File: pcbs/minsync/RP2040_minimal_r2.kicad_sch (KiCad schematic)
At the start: 43 parts, among them J1 SWD_JST, J5 SWD_HEADERS, J6 Conn_01x01_Pin, J7 SSD1306, SW1 SW_Push, U1 NCP1117-3.3_SOT223, U2 W25Q128JVS, U3 RP2040, U4 Si5351A-B-GT, Y2 Crystal_GND24

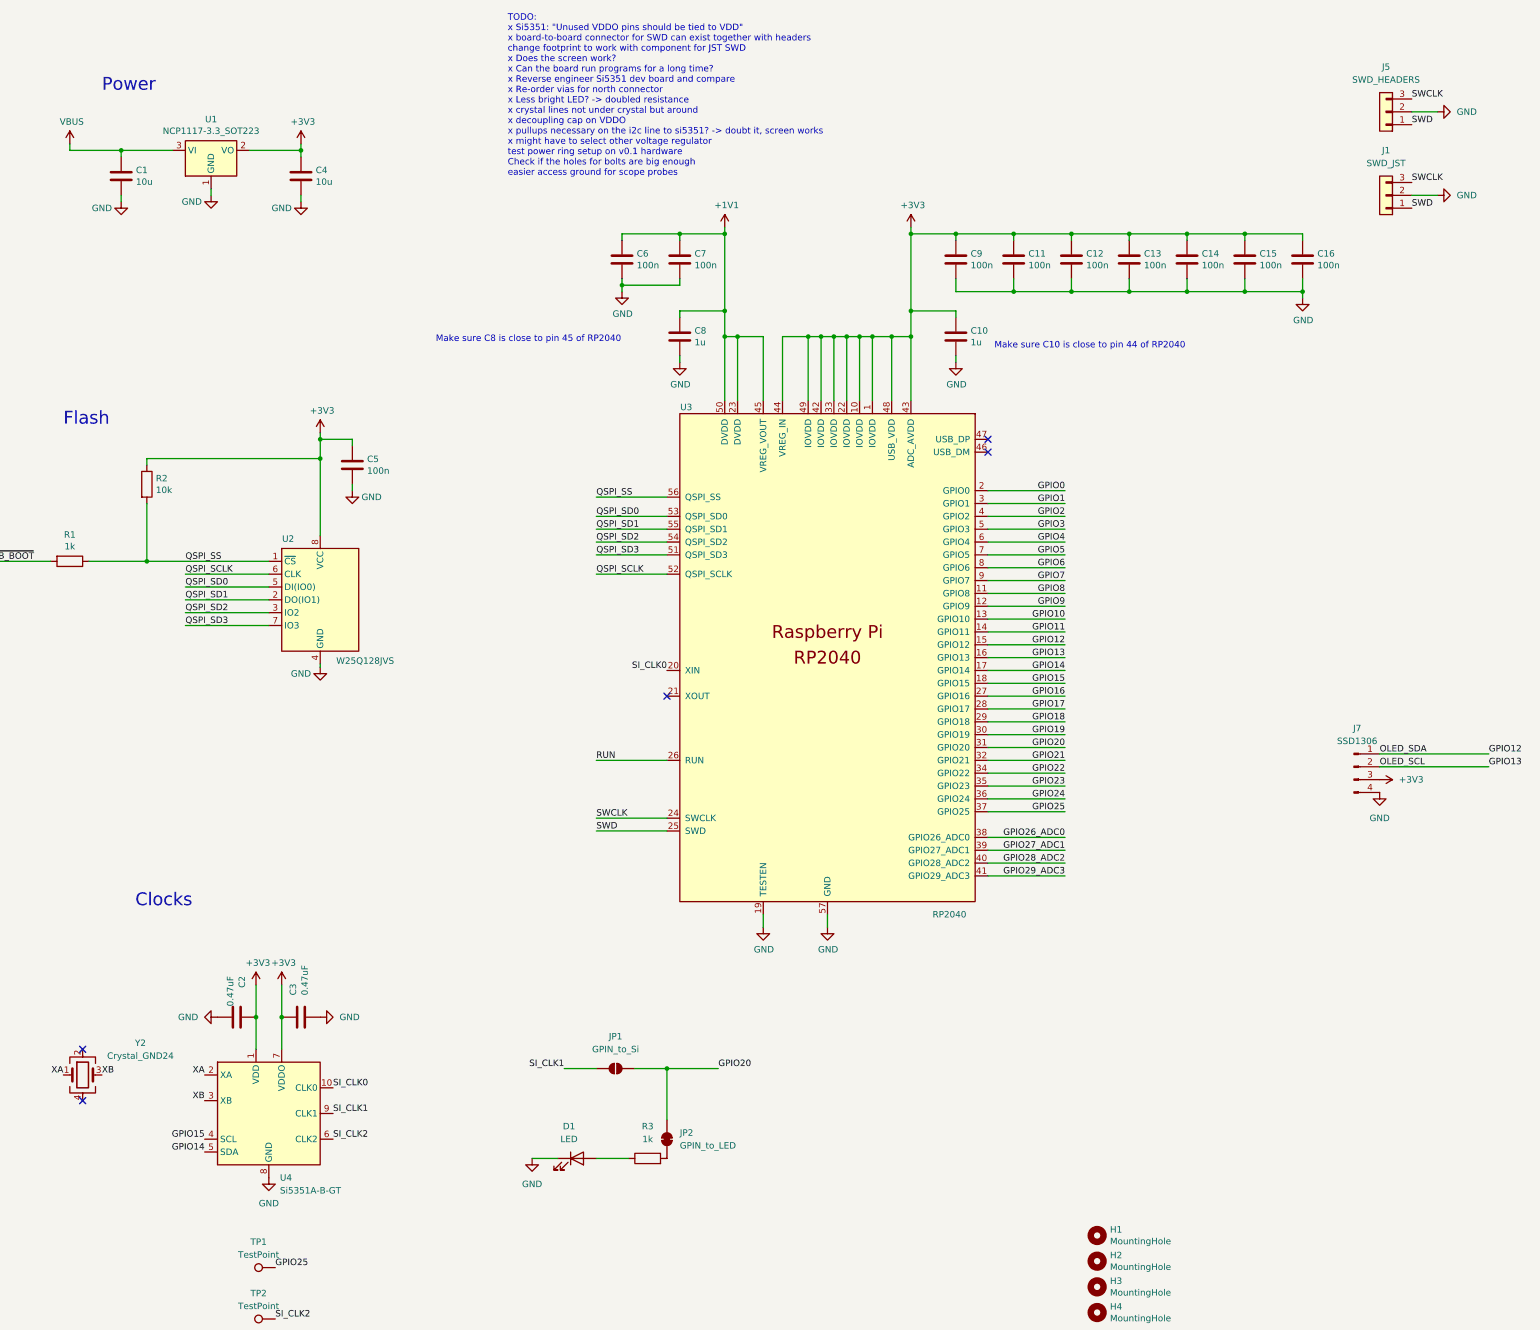
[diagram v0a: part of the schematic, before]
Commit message: Add pullups for si5351, change SWD plug footprint
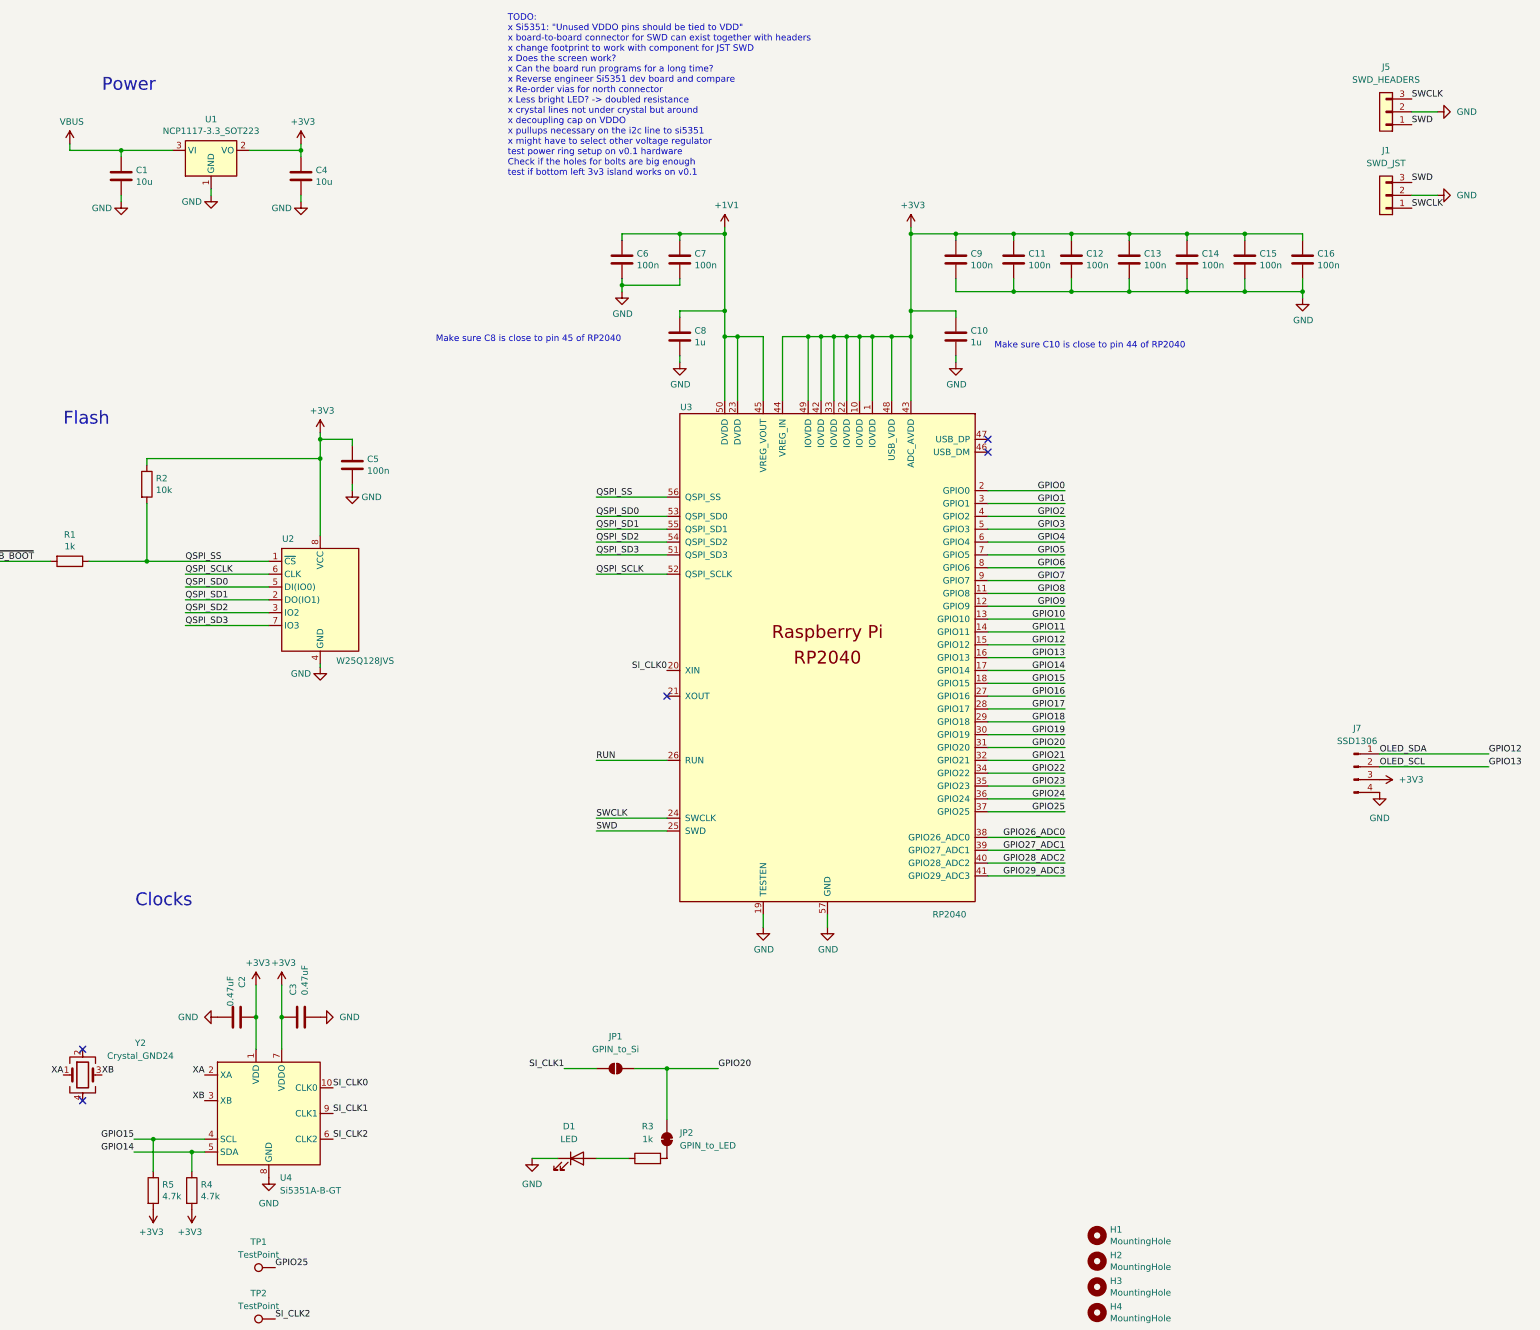
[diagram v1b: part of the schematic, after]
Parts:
- added R4, R5: 4.7k, Resistor_SMD:R_0402_1005Metric, symbol Device:R
- J1: footprint Connector_JST:JST_ACH_BM03B-ACHSS-GAN-ETF_1x03-1MP_P1.20mm_Vertical -> Connector_JST:JST_SH_BM03B-SRSS-TB_1x03-1MP_P1.00mm_Vertical
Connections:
- net +3V3: now also R4.2, R5.2
- net GPIO14: now also R4.1
- net GPIO15: now also R5.1
- net SWCLK: now also J1.1 (Pin_1); no longer J1.3 (Pin_3)
- net SWD: now also J1.3 (Pin_3); no longer J1.1 (Pin_1)
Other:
- note added: "TODO: x Si5351: "Unused VDDO pins should be tied to VDD" x board-to-board connector for SWD can exist together with headers x change footprint to work with component for JST SWD x Does the screen work? x Can the board run programs for a long time? x Reverse engineer Si5351 dev board and compare x Re-order vias for north connector x Less bright LED? -> doubled resistance x crystal lines not under 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"
- note removed: "TODO: x Si5351: "Unused VDDO pins should be tied to VDD" x board-to-board connector for SWD can exist together with headers change footprint to work with component for JST SWD x Does the screen work? x Can the board run programs for a long time? x Reverse engineer Si5351 dev board and compare x Re-order vias for north connector x Less bright LED? -> doubled resistance x crystal lines not under cr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"

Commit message: Try new pitopi connector
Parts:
- removed PTP1, PTP2, PTP3, PTP4: Comm, RP2040_minimal:pitopi_and_power, symbol Connector_Generic:Conn_02x04_Odd_Even
- added PTP1, PTP2, PTP3, PTP4: BM23FR0.6-6DS-0.35V_51_, RP2040_minimal:HRS_BM23FR0.6-6DS-0.35V_51_, symbol BM23FR0.6-6DS-0.35V_51_:BM23FR0.6-6DS-0.35V_51_
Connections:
- net GPIO0: now also PTP1.1
- net GPIO1: now also PTP1.3
- net GPIO10: now also PTP2.4
- net GPIO11: now also PTP2.2
- net GPIO16: now also PTP3.6
- net GPIO17: now also PTP3.4
- net GPIO18: now also PTP3.2
- net GPIO19: now also PTP3.1
- net GPIO2: now also PTP1.5
- net GPIO21: now also PTP3.3
- net GPIO22: now also PTP3.5
- net GPIO23: now also PTP4.6
- net GPIO24: now also PTP4.4
- net GPIO26_ADC0: now also PTP4.2
- net GPIO27_ADC1: now also PTP4.1
- net GPIO28_ADC2: now also PTP4.3
- net GPIO29_ADC3: now also PTP4.5
- net GPIO3: now also PTP1.6
- net GPIO4: now also PTP1.4
- net GPIO5: now also PTP1.2
- net GPIO6: now also PTP2.1
- net GPIO7: now also PTP2.3
- net GPIO8: now also PTP2.5
- net GPIO9: now also PTP2.6

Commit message: Use JST SH headers for pitopi
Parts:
- added J2: POWER, Connector_JST:JST_PH_B2B-PH-SM4-TB_1x02-1MP_P2.00mm_Vertical, symbol Connector:Conn_01x02_Socket
- added J3: POWER, Connector_JST:JST_PH_B2B-PH-SM4-TB_1x02-1MP_P2.00mm_Vertical, symbol Connector:Conn_01x02_Pin
- PTP1, PTP2, PTP3, PTP4: footprint RP2040_minimal:HRS_BM23FR0.6-6DS-0.35V_51_ -> Connector_JST:JST_SH_BM06B-SRSS-TB_1x06-1MP_P1.00mm_Vertical
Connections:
- net GND: now also J2.2 (Pin_2), J3.2 (Pin_2)
- net GPIO0: now also PTP1.6; no longer PTP1.1
- net GPIO1: now also PTP1.5; no longer PTP1.3
- net GPIO10: now also PTP2.2; no longer PTP2.4
- net GPIO11: now also PTP2.1; no longer PTP2.2
- net GPIO17: now also PTP3.5; no longer PTP3.4
- net GPIO18: now also PTP3.4; no longer PTP3.2
- net GPIO19: now also PTP3.3; no longer PTP3.1
- net GPIO2: now also PTP1.4; no longer PTP1.5
- net GPIO21: now also PTP3.2; no longer PTP3.3
- net GPIO22: now also PTP3.1; no longer PTP3.5
- net GPIO24: now also PTP4.5; no longer PTP4.4
- net GPIO26_ADC0: now also PTP4.4; no longer PTP4.2
- net GPIO27_ADC1: now also PTP4.3; no longer PTP4.1
- net GPIO28_ADC2: now also PTP4.2; no longer PTP4.3
- net GPIO29_ADC3: now also PTP4.1; no longer PTP4.5
- net GPIO3: now also PTP1.3; no longer PTP1.6
- net GPIO4: now also PTP1.2; no longer PTP1.4
- net GPIO5: now also PTP1.1; no longer PTP1.2
- net GPIO6: now also PTP2.6; no longer PTP2.1
- net GPIO7: now also PTP2.5; no longer PTP2.3
- net GPIO8: now also PTP2.4; no longer PTP2.5
- net GPIO9: now also PTP2.3; no longer PTP2.6
- net VBUS: now also J2.1 (Pin_1), J3.1 (Pin_1)

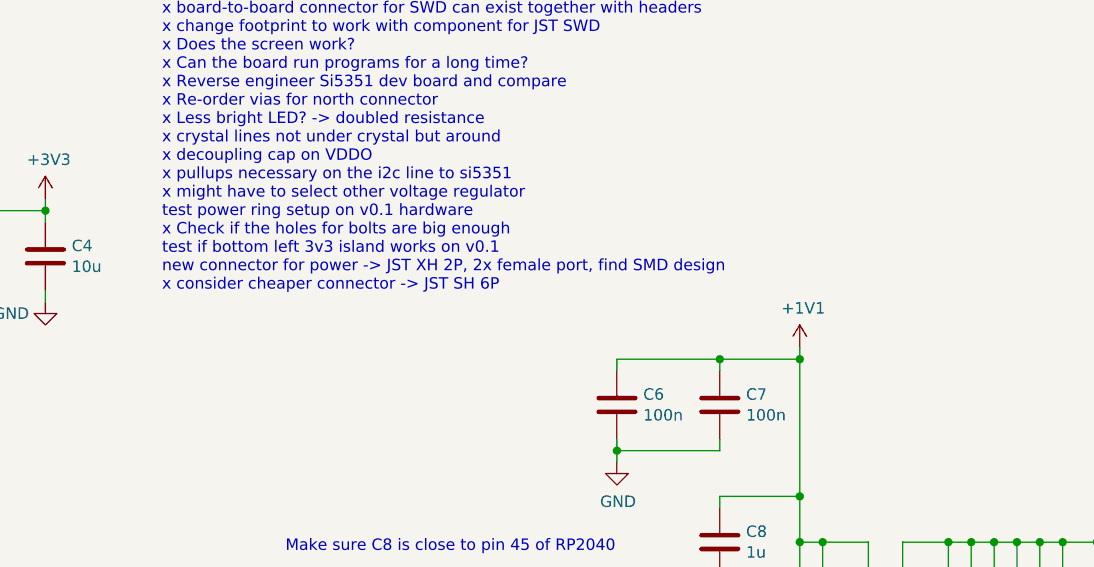
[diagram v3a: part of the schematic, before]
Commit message: Add vias before JST connectors
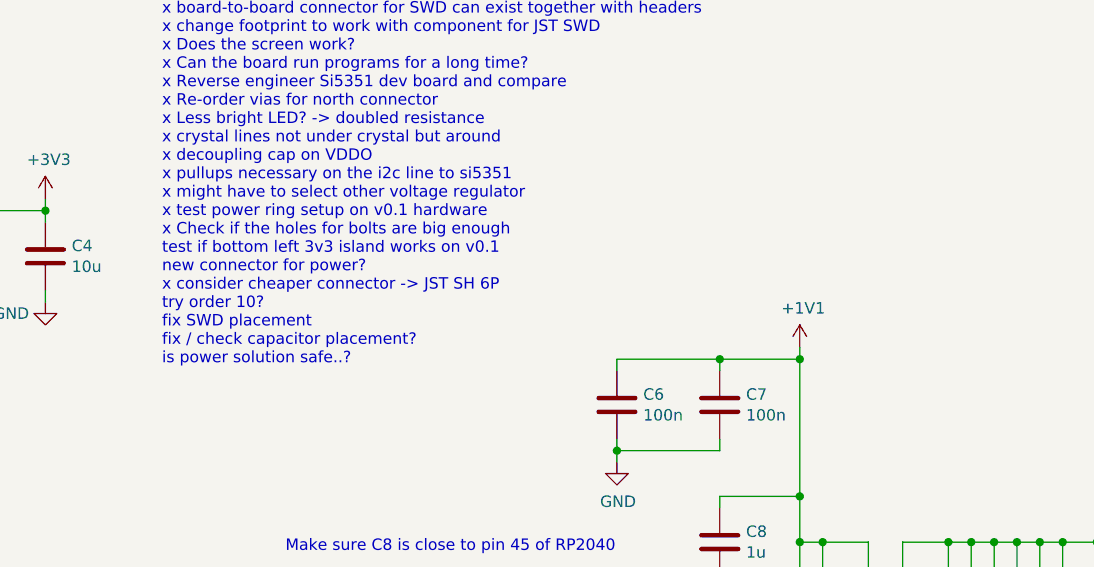
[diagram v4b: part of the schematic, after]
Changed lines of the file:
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@@
 		)
 	)
-	(text "TODO:\nx Si5351: \"Unused VDDO pins should be tied to VDD\"\nx board-to-board connector for SWD can exist together with headers\nx change footprint to work with component for JST SWD\nx Does the screen work?\nx Can the board run programs for a long time?\nx Reverse engineer Si5351 dev board and compare\nx Re-order vias for north connector\nx Less bright LED? -> doubled resistance\nx crystal lines not under crystal but around\nx decoupling cap on VDDO\nx pullups necessary on the i2c line to si5351\nx might have to select other voltage regulator\ntest power ring setup on v0.1 hardware\nx Check if the holes for bolts are big enough\ntest if bottom left 3v3 island works on v0.1\nnew connector for power -> JST XH 2P, 2x female port, find SMD design\nx consider cheaper connector -> JST SH 6P"
+	(text "TODO:\nx Si5351: \"Unused VDDO pins should be tied to VDD\"\nx board-to-board connector for SWD can exist together with headers\nx change footprint to work with component for JST SWD\nx Does the screen work?\nx Can the board run programs for a long time?\nx Reverse engineer Si5351 dev board and compare\nx Re-order vias for north connector\nx Less bright LED? -> doubled resistance\nx crystal lines not under crystal but around\nx decoupling cap on VDDO\nx pullups necessary on the i2c line to si5351\nx might have to select other voltage regulator\nx test power ring setup on v0.1 hardware\nx Check if the holes for bolts are big enough\ntest if bottom left 3v3 island works on v0.1\nnew connector for power?\nx consider cheaper connector -> JST SH 6P\ntry order 10?\nfix SWD placement\nfix / check capacitor placement?\nis power solution safe..?"
 		(exclude_from_sim no)
 		(at 106.934 17.272 0)

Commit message: Update TODO's for minsync v0.2
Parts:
- removed J2: POWER, Connector_JST:JST_PH_B2B-PH-SM4-TB_1x02-1MP_P2.00mm_Vertical, symbol Connector:Conn_01x02_Socket
- J3: footprint Connector_JST:JST_PH_B2B-PH-SM4-TB_1x02-1MP_P2.00mm_Vertical -> Connector_PinHeader_2.54mm:PinHeader_1x02_P2.54mm_Vertical
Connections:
- net GND: now also J3.1 (Pin_1); no longer J3.2 (Pin_2)
- net VBUS: now also J3.2 (Pin_2); no longer J3.1 (Pin_1)
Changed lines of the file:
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@@
 	)
 	(junction
-		(at 38.1 62.23)
-		(diameter 0)
-		(color 0 0 0 0)
-	)
-	(junction
 		(at 168.91 60.96)
 		(diameter 0)
@@
 	)
 	(junction
-		(at 39.37 64.77)
-		(diameter 0)
-		(color 0 0 0 0)
-	)
-	(junction
 		(at 207.01 81.28)
 		(diameter 0)
@@
 	(wire
 		(pts
-			(xy 38.1 62.23) (xy 41.91 62.23)
-		)
-		(stroke
-			(width 0)
-			(type default)
-		)
-	)
-	(wire
-		(pts
 			(xy 64.77 240.03) (xy 64.77 246.38)
 		)
@@
 	(wire
 		(pts
-			(xy 39.37 64.77) (xy 41.91 64.77)
-		)
-		(stroke
-			(width 0)
-			(type default)
-		)
-	)
-	(wire
-		(pts
 			(xy 157.48 62.23) (xy 157.48 60.96)
 		)
@@
 		)
 	)
-	(text "TODO:\nx Si5351: \"Unused VDDO pins should be tied to VDD\"\nx board-to-board connector for SWD can exist together with headers\nx change footprint to work with component for JST SWD\nx Does the screen work?\nx Can the board run programs for a long time?\nx Reverse engineer Si5351 dev board and compare\nx Re-order vias for north connector\nx Less bright LED? -> doubled resistance\nx crystal lines not under crystal but around\nx decoupling cap on VDDO\nx pullups necessary on the i2c line to si5351\nx might have to select other voltage regulator\nx test power ring setup on v0.1 hardware\nx Check if the holes for bolts are big enough\ntest if bottom left 3v3 island works on v0.1\nnew connector for power?\nx consider cheaper connector -> JST SH 6P\ntry order 10?\nfix SWD placement\nfix / check capacitor placement?\nis power solution safe..?"
+	(text "TODO:\nx Si5351: \"Unused VDDO pins should be tied to VDD\"\nx board-to-board connector for SWD can exist together with headers\nx change footprint to work with component for JST SWD\nx Does the screen work?\nx Can the board run programs for a long time?\nx Reverse engineer Si5351 dev board and compare\nx Re-order vias for north connector\nx Less bright LED? -> doubled resistance\nx crystal lines not under crystal but around\nx decoupling cap on VDDO\nx pullups necessary on the i2c line to si5351\nx might have to select other voltage regulator\nx test power ring setup on v0.1 hardware\nx Check if the holes for bolts are big enough\ntest if bottom left 3v3 island works on v0.1\nnew connector for power?\nx consider cheaper connector -> JST SH 6P\nx try order 10? -> ~20 euros more expensive"
 		(exclude_from_sim no)
 		(at 106.934 17.272 0)
@@
 	(symbol
 		(lib_id "power:GND")
-		(at 39.37 64.77 0)
+		(at 38.1 62.23 180)
 		(unit 1)
 		(exclude_from_sim no)
@@
 		(dnp no)
 		(property "Reference" "#PWR021"
-			(at 39.37 71.12 0)
+			(at 38.1 55.88 0)
 			(effects
 				(font
@@
 		)
 		(property "Value" "GND"
-			(at 35.56 66.04 0)
+			(at 41.91 60.96 0)
 			(effects
 				(font
@@
 		)
 		(property "Footprint" ""
-			(at 39.37 64.77 0)
+			(at 38.1 62.23 0)
 			(effects
 				(font
@@
 		)
 		(property "Datasheet" ""
-			(at 39.37 64.77 0)
+			(at 38.1 62.23 0)
 			(effects
 				(font
@@
 		)
 		(property "Description" ""
-			(at 39.37 64.77 0)
+			(at 38.1 62.23 0)
 			(effects
 				(font
@@
 			)
 		)
-		(property "Footprint" "Connector_JST:JST_PH_B2B-PH-SM4-TB_1x02-1MP_P2.00mm_Vertical"
+		(property "Footprint" "Connector_PinHeader_2.54mm:PinHeader_1x02_P2.54mm_Vertical"
 			(at 30.48 62.23 0)
 			(effects
@@
 	)
 	(symbol
-		(lib_id "Connector:Conn_01x02_Socket")
-		(at 46.99 62.23 0)
-		(unit 1)
-		(exclude_from_sim no)
-		(in_bom yes)
-		(on_board yes)
-		(dnp no)
-		(fields_autoplaced yes)
-		(property "Reference" "J2"
-			(at 48.26 62.2299 0)
-			(effects
-				(font
-					(size 1.27 1.27)
-				)
-				(justify left)
-			)
-		)
-		(property "Value" "POWER"
-			(at 48.26 64.7699 0)
-			(effects
-				(font
-					(size 1.27 1.27)
-				)
-				(justify left)
-			)
-		)
-		(property "Footprint" "Connector_JST:JST_PH_B2B-PH-SM4-TB_1x02-1MP_P2.00mm_Vertical"
-			(at 46.99 62.23 0)
-			(effects
-				(font
-					(size 1.27 1.27)
-				)
-				(hide yes)
-			)
-		)
-		(property "Datasheet" "~"
-			(at 46.99 62.23 0)
-			(effects
-				(font
-					(size 1.27 1.27)
-				)
-				(hide yes)
-			)
-		)
-		(property "Description" "Generic connector, single row, 01x02, script generated"
-			(at 46.99 62.23 0)
-			(effects
-				(font
-					(size 1.27 1.27)
-				)
-				(hide yes)
-			)
-		)
-		(pin "2"
-		)
-		(pin "1"
-		)
-		(instances
-			(project ""
-				(path "/8c0b3d8b-46d3-4173-ab1e-a61765f77d61"
-					(reference "J2")
-					(unit 1)
-				)
-			)
-		)
-	)
-	(symbol
 		(lib_id "BM23FR0.6-6DS-0.35V_51_:BM23FR0.6-6DS-0.35V_51_")
 		(at 379.73 82.55 0)
@@
 	(symbol
 		(lib_id "power:VBUS")
-		(at 38.1 62.23 0)
+		(at 39.37 64.77 180)
 		(unit 1)
 		(exclude_from_sim no)
@@
 		(dnp no)
 		(property "Reference" "#PWR022"
-			(at 38.1 66.04 0)
+			(at 39.37 60.96 0)
 			(effects
 				(font
@@
 		)
 		(property "Value" "VBUS"
-			(at 38.481 57.8358 0)
+			(at 38.989 69.1642 0)
 			(effects
 				(font
@@
 		)
 		(property "Footprint" ""
-			(at 38.1 62.23 0)
+			(at 39.37 64.77 0)
 			(effects
 				(font
@@
 		)
 		(property "Datasheet" ""
-			(at 38.1 62.23 0)
+			(at 39.37 64.77 0)
 			(effects
 				(font
@@
 		)
 		(property "Description" ""
-			(at 38.1 62.23 0)
+			(at 39.37 64.77 0)
 			(effects
 				(font

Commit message: Productionize minsync v0.2
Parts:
- C2, C3: footprint Capacitor_SMD:C_0402_1005Metric -> Capacitor_SMD:C_0603_1608Metric
- R4, R5: value 4.7k -> 2.2k
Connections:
- net XA: now also Y2.3; no longer Y2.1
- net XB: now also Y2.1; no longer Y2.3
